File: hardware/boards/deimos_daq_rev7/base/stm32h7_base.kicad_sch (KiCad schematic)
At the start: 2 parts

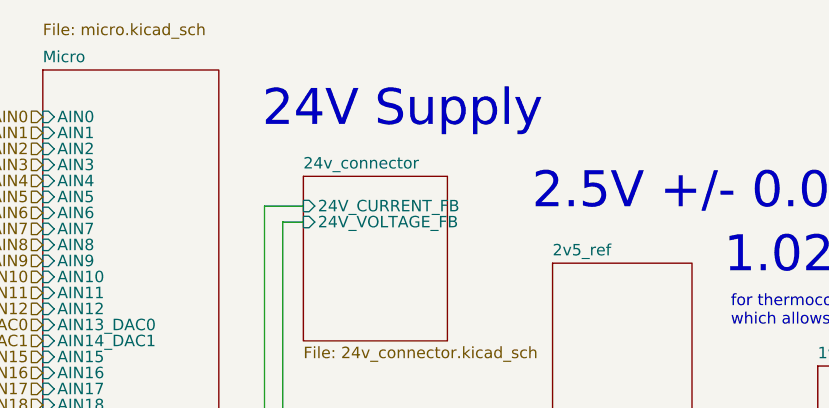
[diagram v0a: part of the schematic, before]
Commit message: wip to export more gpio pins
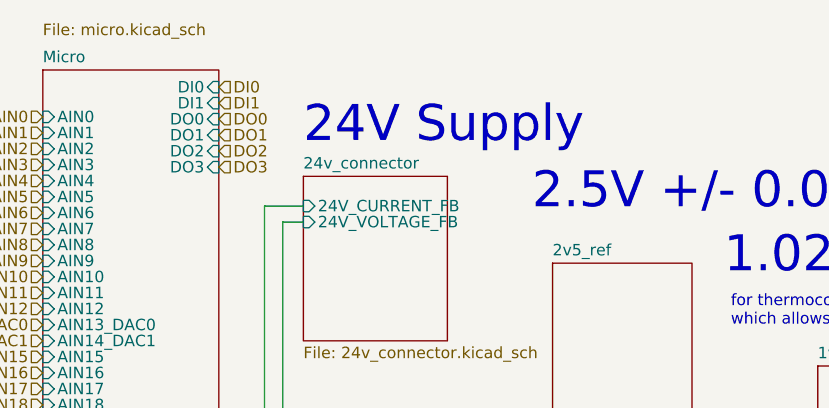
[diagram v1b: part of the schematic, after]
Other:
- sheet Micro ports: added DI0, DI1, DO0, DO1, DO2, DO3; removed none
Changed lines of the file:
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@@
 	(text "24V Supply"
 		(exclude_from_sim no)
-		(at 50.8 25.146 0)
+		(at 55.372 26.924 0)
 		(effects
 			(font
@@
 		)
 	)
+	(hierarchical_label "DI0"
+		(shape input)
+		(at 45.974 20.32 0)
+		(effects
+			(font
+				(size 1.27 1.27)
+			)
+			(justify left)
+		)
+	)
 	(hierarchical_label "PWM3"
 		(shape input)
@@
 		)
 	)
+	(hierarchical_label "DI1"
+		(shape input)
+		(at 45.974 22.098 0)
+		(effects
+			(font
+				(size 1.27 1.27)
+			)
+			(justify left)
+		)
+	)
 	(hierarchical_label "PWM1"
 		(shape input)
@@
 		)
 	)
+	(hierarchical_label "DO1"
+		(shape input)
+		(at 45.974 25.654 0)
+		(effects
+			(font
+				(size 1.27 1.27)
+			)
+			(justify left)
+		)
+	)
 	(hierarchical_label "PWM0"
 		(shape input)
@@
 		)
 	)
+	(hierarchical_label "DO2"
+		(shape input)
+		(at 45.974 27.432 0)
+		(effects
+			(font
+				(size 1.27 1.27)
+			)
+			(justify left)
+		)
+	)
 	(hierarchical_label "PWM2"
 		(shape input)
@@
 		)
 	)
+	(hierarchical_label "DO3"
+		(shape input)
+		(at 45.974 29.21 0)
+		(effects
+			(font
+				(size 1.27 1.27)
+			)
+			(justify left)
+		)
+	)
 	(hierarchical_label "AIN12"
 		(shape input)
@@
 			)
 			(justify right)
+		)
+	)
+	(hierarchical_label "DO0"
+		(shape input)
+		(at 45.974 23.876 0)
+		(effects
+			(font
+				(size 1.27 1.27)
+			)
+			(justify left)
 		)
 	)
@@
 			)
 		)
+		(pin "DI1" input
+			(at 45.974 22.098 0)
+			(effects
+				(font
+					(size 1.27 1.27)
+				)
+				(justify right)
+			)
+		)
+		(pin "DI0" input
+			(at 45.974 20.32 0)
+			(effects
+				(font
+					(size 1.27 1.27)
+				)
+				(justify right)
+			)
+		)
+		(pin "DO0" input
+			(at 45.974 23.876 0)
+			(effects
+				(font
+					(size 1.27 1.27)
+				)
+				(justify right)
+			)
+		)
+		(pin "DO2" input
+			(at 45.974 27.432 0)
+			(effects
+				(font
+					(size 1.27 1.27)
+				)
+				(justify right)
+			)
+		)
+		(pin "DO1" input
+			(at 45.974 25.654 0)
+			(effects
+				(font
+					(size 1.27 1.27)
+				)
+				(justify right)
+			)
+		)
+		(pin "DO3" input
+			(at 45.974 29.21 0)
+			(effects
+				(font
+					(size 1.27 1.27)
+				)
+				(justify right)
+			)
+		)
